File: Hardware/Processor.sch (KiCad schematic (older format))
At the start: 33 parts, among them J1 ICSP-CORTEX, J3 CONN-9, U6 STM32L100RBT6, U9 LM2903DT, X1 8MHz

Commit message: Replace comparator with SSOP version
Closes #3
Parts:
- U9: Distributor Part No 497-1559-1-ND -> 296-16806-1-ND; MFR Name ST -> TI; MFR Part No LM2903DT -> LM2903DGKR
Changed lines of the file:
@@
 Sheet 3 5
 Title "Solid State Cosmic Ray Detector"
-Date "11 sep 2014"
+Date "12 sep 2014"
 Rev "1"
 Comp "Ethan Harstad"
@@
 F 2 "~" H 5500 3800 60  0000 C CNN
 F 3 "~" H 5500 3800 60  0000 C CNN
-F 4 "ST" H 5500 3800 60  0001 C CNN "MFR Name"
-F 5 "LM2903DT" H 5500 3800 60  0001 C CNN "MFR Part No"
-F 6 "497-1559-1-ND" H 5500 3800 60  0001 C CNN "Distributor Part No"
+F 4 "TI" H 5500 3800 60  0001 C CNN "MFR Name"
+F 5 "LM2903DGKR" H 5500 3800 60  0001 C CNN "MFR Part No"
+F 6 "296-16806-1-ND" H 5500 3800 60  0001 C CNN "Distributor Part No"
 	1    5500 3800
 	1    0    0    -1
@@
 Wire Wire Line
 	4000 1500 3900 1500
-$Comp
-L OPAMP-DUAL U9
-U 2 1 541203DD
-P 7600 3800
-F 0 "U9" H 7350 3900 50  0000 L CNN
-F 1 "LM2903DT" H 7350 3800 50  0000 L CNN
-F 2 "~" H 7600 3800 60  0000 C CNN
-F 3 "~" H 7600 3800 60  0000 C CNN
-F 4 "ST" H 7600 3800 60  0001 C CNN "MFR Name"
-F 5 "LM2903DT" H 7600 3800 60  0001 C CNN "MFR Part No"
-F 6 "497-1559-1-ND" H 7600 3800 60  0001 C CNN "Distributor Part No"
-	2    7600 3800
-	1    0    0    -1
-$EndComp
 Wire Wire Line
 	5500 4200 5500 4300
@@
 	7900 5400 7700 5400
 Connection ~ 7700 5400
+$Comp
+L OPAMP-DUAL U9
+U 2 1 541324C2
+P 7600 3800
+F 0 "U9" H 7350 3900 50  0000 L CNN
+F 1 "LM2903DT" H 7350 3800 50  0000 L CNN
+F 2 "~" H 7600 3800 60  0000 C CNN
+F 3 "~" H 7600 3800 60  0000 C CNN
+F 4 "TI" H 7600 3800 60  0001 C CNN "MFR Name"
+F 5 "LM2903DGKR" H 7600 3800 60  0001 C CNN "MFR Part No"
+F 6 "296-16806-1-ND" H 7600 3800 60  0001 C CNN "Distributor Part No"
+	2    7600 3800
+	1    0    0    -1
+$EndComp
 $EndSCHEMATC

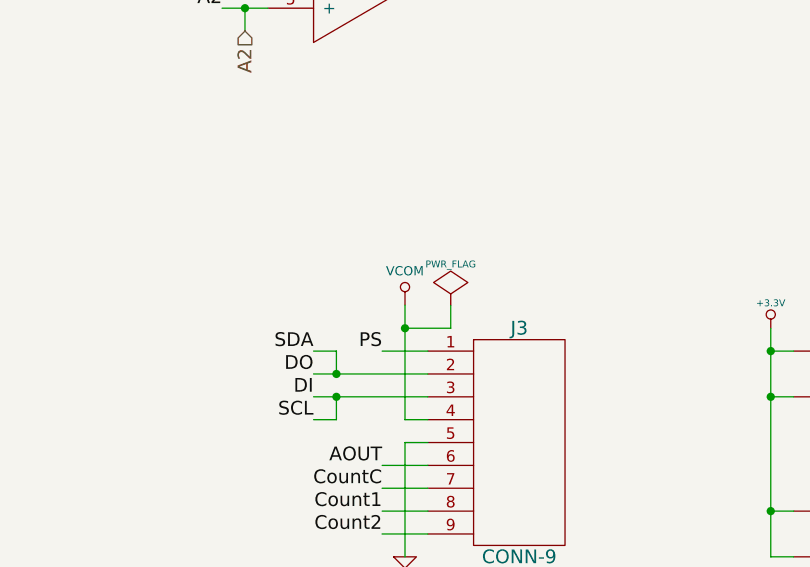
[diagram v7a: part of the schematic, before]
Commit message: Replace boost converter
Closes #4
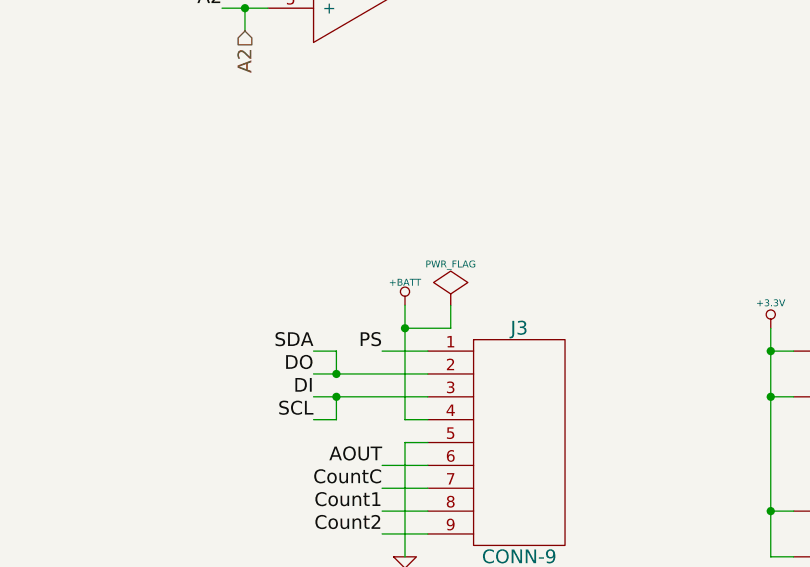
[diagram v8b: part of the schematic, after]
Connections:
- net VCOM renamed +BATT
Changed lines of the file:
@@
 Sheet 3 5
 Title "Solid State Cosmic Ray Detector"
-Date "12 sep 2014"
+Date "22 sep 2014"
 Rev "1"
 Comp "Ethan Harstad"
@@
 F 3 "" H 7700 6400 60  0000 C CNN
 	1    7700 6400
-	1    0    0    -1
-$EndComp
-$Comp
-L VCOM #PWR57
-U 1 1 52B50CC7
-P 7700 5300
-F 0 "#PWR57" H 7700 5500 40  0001 C CNN
-F 1 "VCOM" H 7700 5450 40  0000 C CNN
-F 2 "" H 7700 5300 60  0000 C CNN
-F 3 "" H 7700 5300 60  0000 C CNN
-	1    7700 5300
 	1    0    0    -1
 $EndComp
@@
 	1    0    0    -1
 $EndComp
+$Comp
+L +BATT #PWR?
+U 1 1 5420A073
+P 7700 5300
+F 0 "#PWR?" H 7700 5250 20  0001 C CNN
+F 1 "+BATT" H 7700 5400 30  0000 C CNN
+F 2 "" H 7700 5300 60  0000 C CNN
+F 3 "" H 7700 5300 60  0000 C CNN
+	1    7700 5300
+	1    0    0    -1
+$EndComp
